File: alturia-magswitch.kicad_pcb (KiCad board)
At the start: 2 copper layers, 12 x 17.5 mm, 20 parts, among them J101 Conn_01x01, J102 Conn_01x01, J103 Conn_01x01, J104 Conn_01x01, Q101 SISS27ADN-T1-GE3, Q102 Q_NMOS_GSD, U101 DRV5032FB, U102 AP7383-33WR-7, U103 ATtiny4-TS

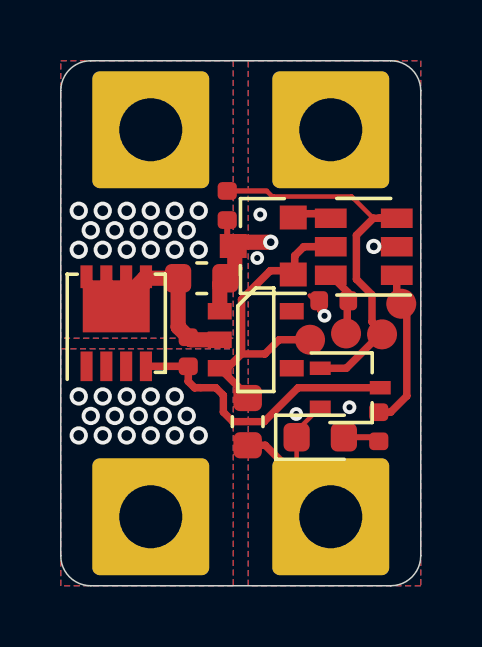
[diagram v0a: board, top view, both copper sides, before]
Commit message: fix wrongly connected power mosfet
Signed-off-by: Thomas Schmid <tom@binary-kitchen.de>
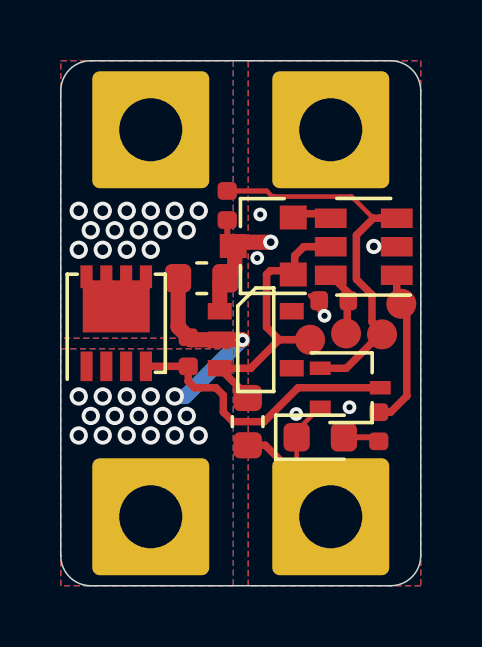
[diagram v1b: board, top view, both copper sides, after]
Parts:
- R102: value 1k -> 10k
- turned J102 to 90 degrees
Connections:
- J101 pad 1: VPP -> OUT
- J102 pad 1: OUT -> VPP
- Q101 pad 1: OUT -> VPP
- Q101 pad 2: OUT -> VPP
- Q101 pad 3: OUT -> VPP
- Q101 pad 5: VPP -> OUT
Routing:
- net VPP: track 5.64 -> 6.99 mm
- net +3V3: track 10.7 -> 10.0 mm
- net OUT: vias 16 -> 15
